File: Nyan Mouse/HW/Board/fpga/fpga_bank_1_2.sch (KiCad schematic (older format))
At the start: 2 parts

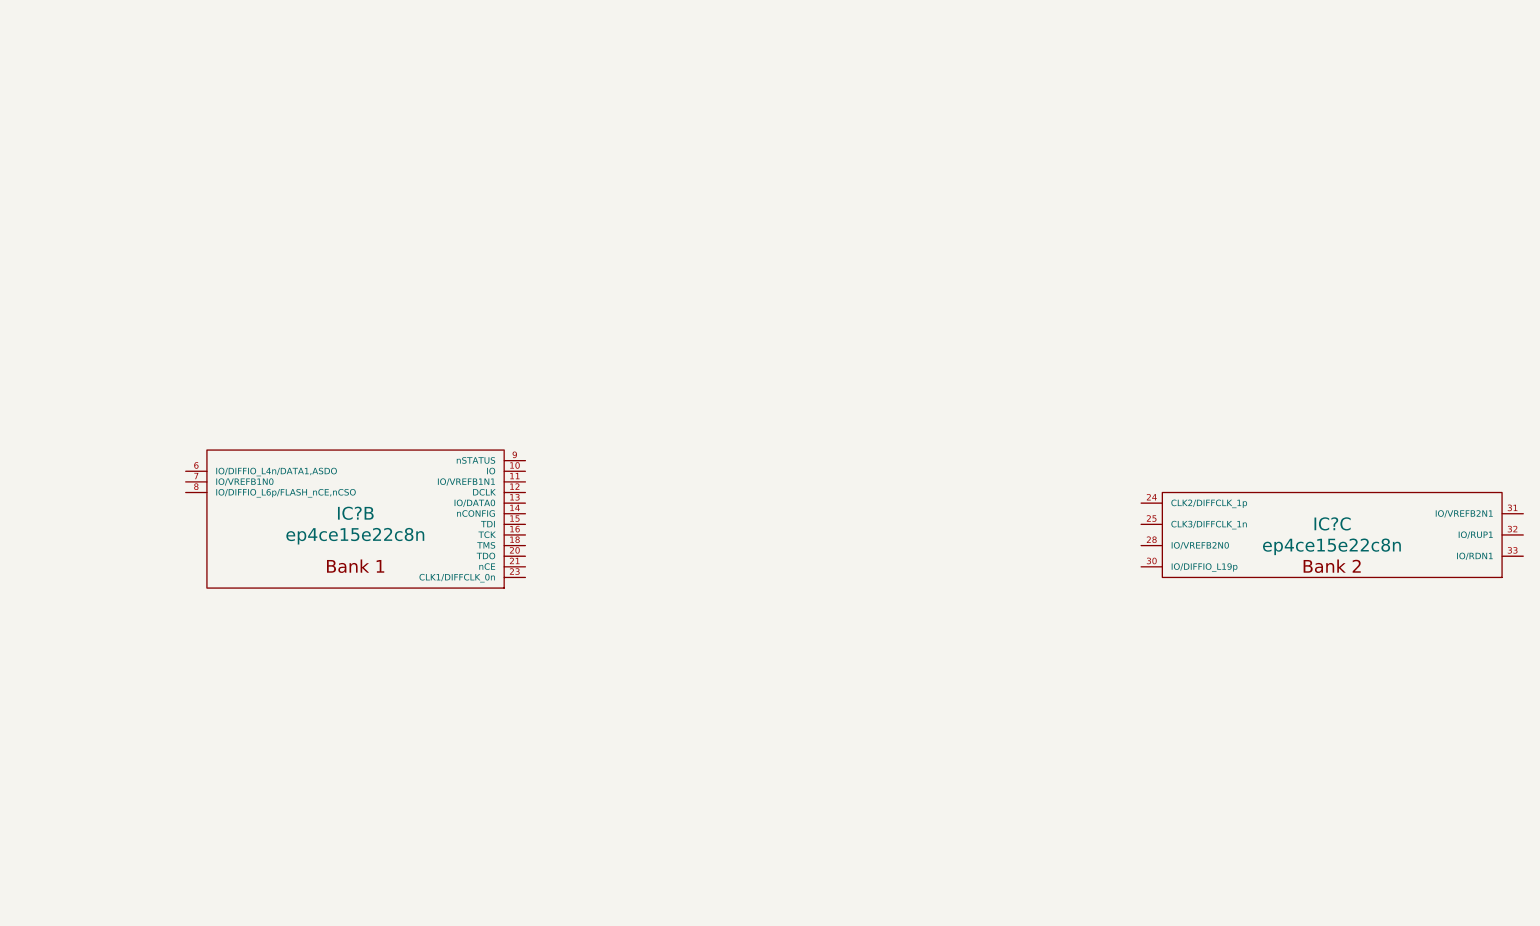
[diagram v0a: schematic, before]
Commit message: Added ESD prevention documentation.
Added ByteBlaster documentation.

Modified FPGA banks.
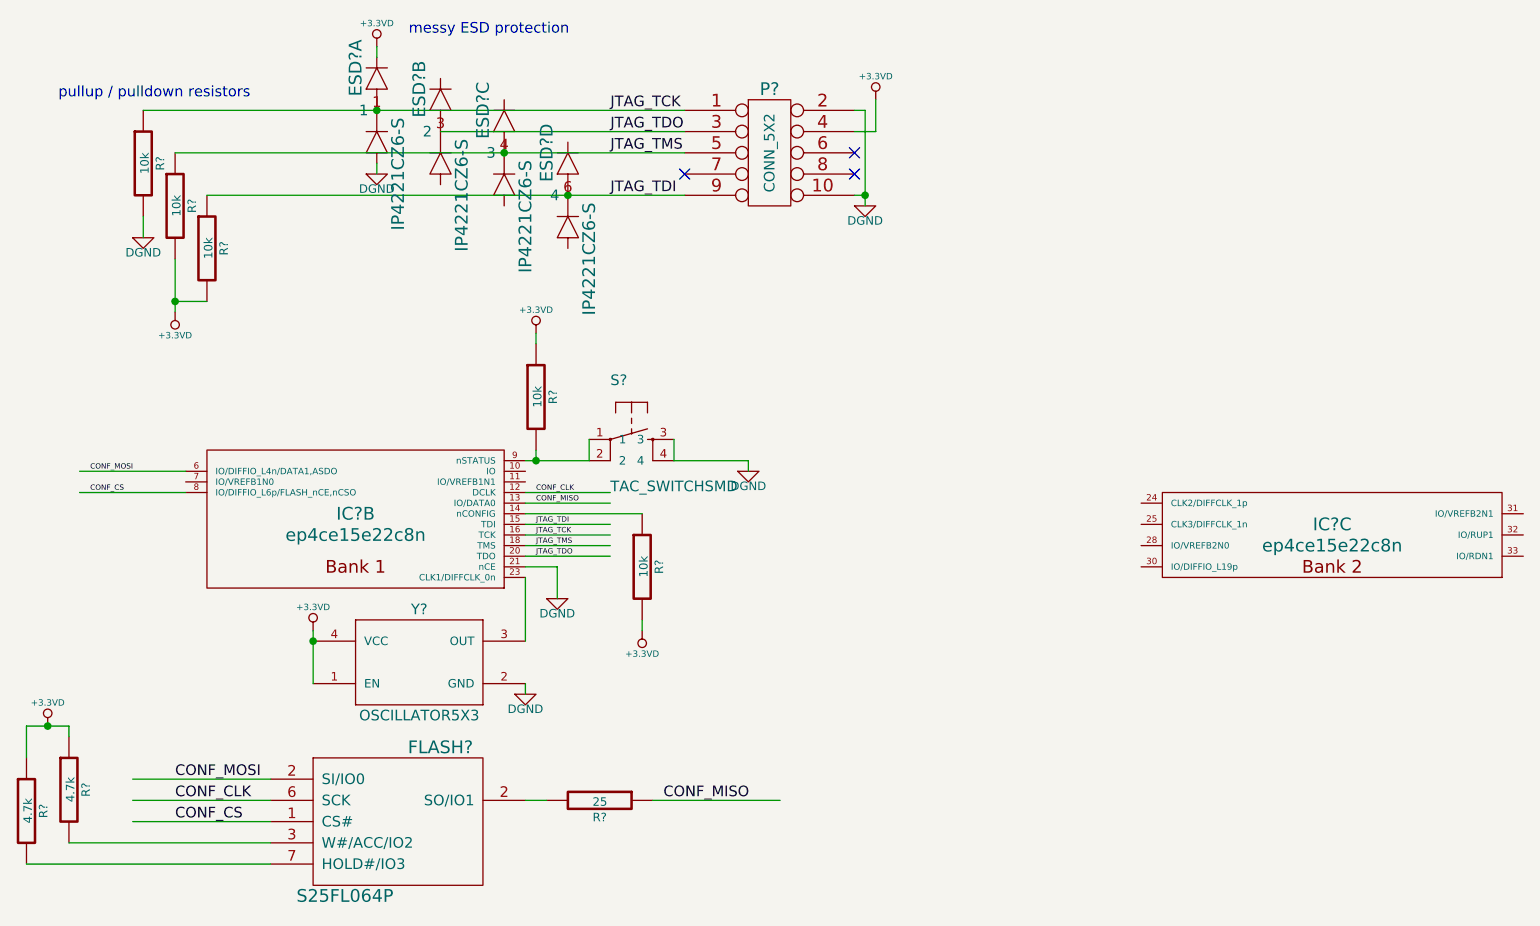
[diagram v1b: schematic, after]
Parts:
- added ESD? (x4): IP4221CZ6-S, symbol IP4221CZ6-S
- added FLASH?: S25FL064P, symbol S25FL064P
- added P?: CONN_5X2, symbol CONN_5X2
- added R? (x5): 10k, symbol R
- added R?: 25, symbol R
- added R? (x2): 4.7k, symbol R
- added S?: TAC_SWITCHSMD, SparkFun-TACTILE_SWITCH_SMD, symbol TAC_SWITCHSMD
- added Y?: OSCILLATOR5X3, SparkFun-CRYSTAL-SMD-5X3, symbol OSCILLATOR5X3
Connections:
- net labels added: +3.3VD, CONF_CLK, CONF_CS, CONF_MISO, CONF_MOSI, DGND, JTAG_TCK, JTAG_TDI, JTAG_TDO, JTAG_TMS
- wire segments 0 -> 46
- no-connect marks 0 -> 3
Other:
- note added: "messy ESD protection"
- note added: "pullup / pulldown resistors"
